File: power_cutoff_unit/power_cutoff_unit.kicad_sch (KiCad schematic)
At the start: 31 parts, among them J1 Conn_01x02, J2 Conn_01x02, J3 Conn_01x02, K1 T9GS1L14-5, U2 STM32F303K8Tx, U3 LMR50410Y5FQDBVRQ1, U4 LMR50410Y3FQDBVRQ1, U5 ADuM120N, U6 MIC4427, U7 MCP2562-E-SN

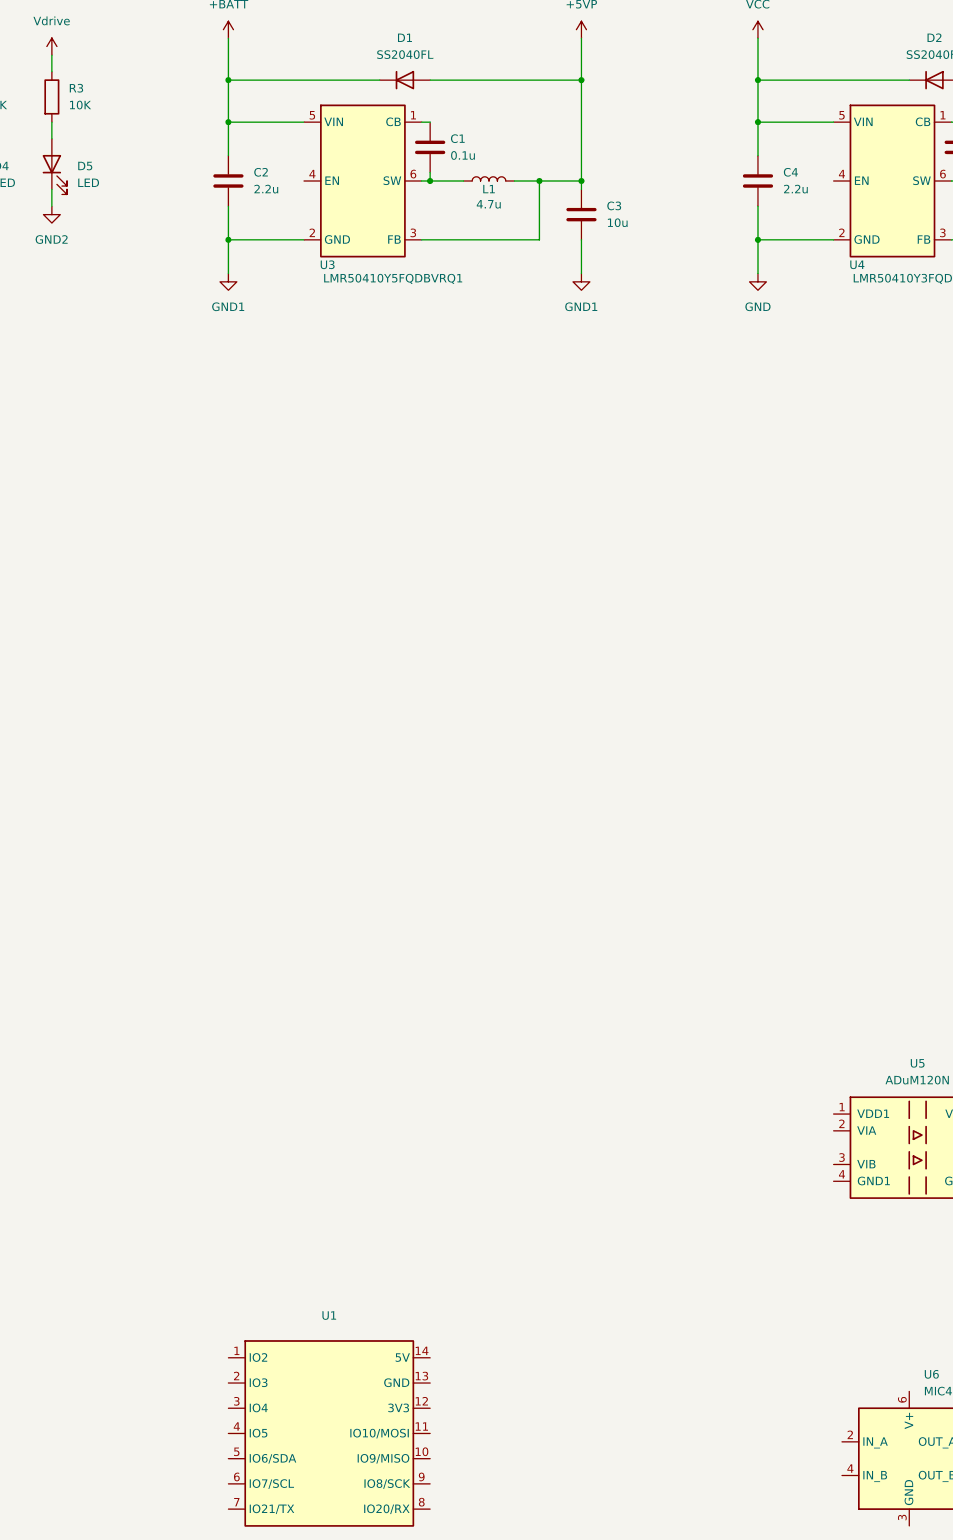
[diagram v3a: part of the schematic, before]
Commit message: 仕様書追記。リレーの追加。
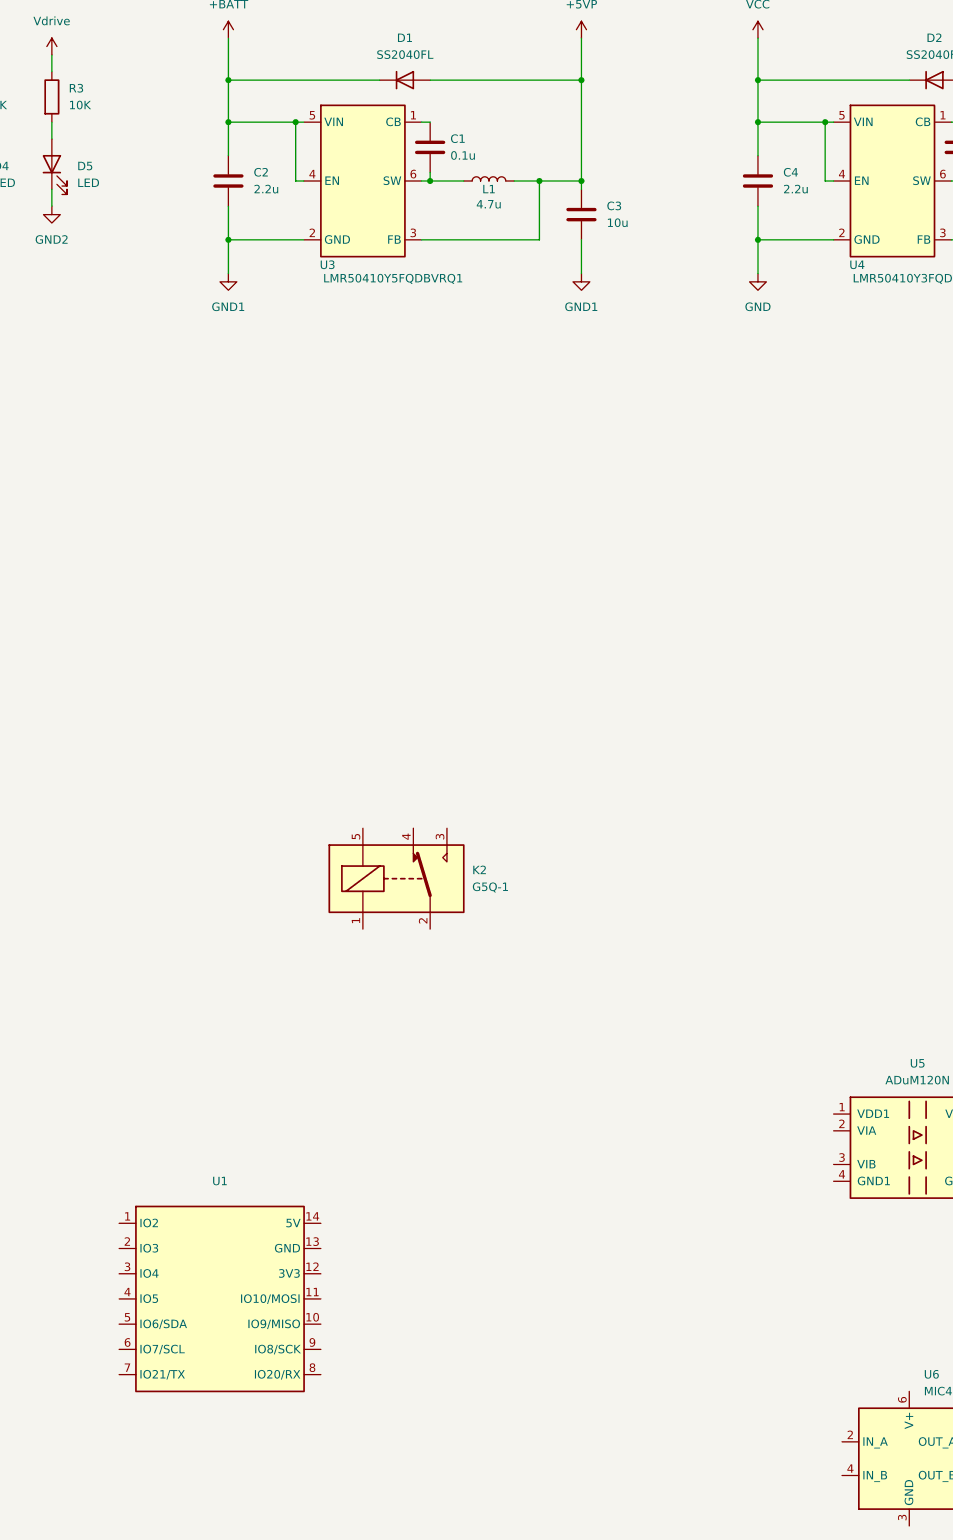
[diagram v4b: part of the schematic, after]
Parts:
- added K2: G5Q-1, Relay_THT:Relay_SPDT_Omron-G5Q-1, symbol Relay:G5Q-1
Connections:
- net +BATT: now also U3.4 (EN)
- net VCC: now also U4.4 (EN)
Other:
- moved on the sheet: U1
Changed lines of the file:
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@@
+	)
+	(junction
+		(at 243.84 38.1)
+		(diameter 0)
+		(color 0 0 0 0)
 	)
 	(junction
@@
 	)
 	(junction
+		(at 163.83 38.1)
+		(diameter 0)
+		(color 0 0 0 0)
+	)
+	(junction
 		(at 287.02 31.75)
 		(diameter 0)
@@
 	(wire
 		(pts
-			(xy 153.67 38.1) (xy 165.1 38.1)
+			(xy 153.67 38.1) (xy 163.83 38.1)
 		)
 		(stroke
@@
 	(wire
 		(pts
+			(xy 163.83 46.99) (xy 163.83 38.1)
+		)
+		(stroke
+			(width 0)
+			(type default)
+		)
+	)
+	(wire
+		(pts
 			(xy 262.89 55.88) (xy 280.67 55.88)
 		)
@@
 	(wire
 		(pts
+			(xy 243.84 38.1) (xy 245.11 38.1)
+		)
+		(stroke
+			(width 0)
+			(type default)
+		)
+	)
+	(wire
+		(pts
 			(xy 184.15 45.72) (xy 184.15 46.99)
 		)
@@
 	(wire
 		(pts
+			(xy 163.83 38.1) (xy 165.1 38.1)
+		)
+		(stroke
+			(width 0)
+			(type default)
+		)
+	)
+	(wire
+		(pts
 			(xy 102.87 27.94) (xy 102.87 30.48)
 		)
@@
 	(wire
 		(pts
+			(xy 243.84 46.99) (xy 243.84 38.1)
+		)
+		(stroke
+			(width 0)
+			(type default)
+		)
+	)
+	(wire
+		(pts
+			(xy 245.11 46.99) (xy 243.84 46.99)
+		)
+		(stroke
+			(width 0)
+			(type default)
+		)
+	)
+	(wire
+		(pts
+			(xy 165.1 46.99) (xy 163.83 46.99)
+		)
+		(stroke
+			(width 0)
+			(type default)
+		)
+	)
+	(wire
+		(pts
 			(xy 64.77 43.18) (xy 64.77 48.26)
 		)
@@
 	(wire
 		(pts
-			(xy 233.68 38.1) (xy 245.11 38.1)
+			(xy 233.68 38.1) (xy 243.84 38.1)
 		)
 		(stroke
@@
 	)
 	(symbol
+		(lib_id "Relay:G5Q-1")
+		(at 179.07 152.4 0)
+		(unit 1)
+		(exclude_from_sim no)
+		(in_bom yes)
+		(on_board yes)
+		(dnp no)
+		(fields_autoplaced yes)
+		(property "Reference" "K2"
+			(at 190.5 151.1299 0)
+			(effects
+				(font
+					(size 1.27 1.27)
+				)
+				(justify left)
+			)
+		)
+		(property "Value" "G5Q-1"
+			(at 190.5 153.6699 0)
+			(effects
+				(font
+					(size 1.27 1.27)
+				)
+				(justify left)
+			)
+		)
+		(property "Footprint" "Relay_THT:Relay_SPDT_Omron-G5Q-1"
+			(at 190.5 153.67 0)
+			(effects
+				(font
+					(size 1.27 1.27)
+				)
+				(justify left)
+				(hide yes)
+			)
+		)
+		(property "Datasheet" "https://www.omron.com/ecb/products/pdf/en-g5q.pdf"
+			(at 179.07 152.4 0)
+			(effects
+				(font
+					(size 1.27 1.27)
+				)
+				(justify left)
+				(hide yes)
+			)
+		)
+		(property "Description" "Omron G5G relay, Miniature Single Pole, SPDT, 10A"
+			(at 179.07 152.4 0)
+			(effects
+				(font
+					(size 1.27 1.27)
+				)
+				(hide yes)
+			)
+		)
+		(pin "4"
+		)
+		(pin "2"
+		)
+		(pin "1"
+		)
+		(pin "5"
+		)
+		(pin "3"
+		)
+		(instances
+			(project ""
+				(path "/24fe50da-72e0-4baa-9f8a-567f58795612"
+					(reference "K2")
+					(unit 1)
+				)
+			)
+		)
+	)
+	(symbol
 		(lib_id "Seed_XIAO:XIAO_ESP32C3")
-		(at 168.91 236.22 0)
+		(at 152.4 215.9 0)
 		(unit 1)
 		(exclude_from_sim no)
@@
 		(fields_autoplaced yes)
 		(property "Reference" "U1"
-			(at 168.91 218.44 0)
+			(at 152.4 198.12 0)
 			(effects
 				(font
@@
 		)
 		(property "Value" "~"
-			(at 168.91 220.98 0)
+			(at 152.4 200.66 0)
 			(effects
 				(font
@@
 		)
 		(property "Footprint" "RF_Module:MCU_Seeed_ESP32C3"
-			(at 162.56 231.14 0)
+			(at 146.05 210.82 0)
 			(effects
 				(font
@@
 		)
 		(property "Datasheet" ""
-			(at 162.56 231.14 0)
+			(at 146.05 210.82 0)
 			(effects
 				(font
@@
 		)
 		(property "Description" ""
-			(at 162.56 231.14 0)
-			(effects
-				(font
+			(at 146.05 210.82 0)
+			(effects
+				(font

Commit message: リレーの回路を組み立てた。
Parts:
- added C10, C8: C_Polarized, symbol Device:C_Polarized
- added C11, C12, C7, C9: C, symbol Device:C
- added D10, D12, D13, D9: LED, symbol Device:LED
- added D11, D8: D, symbol Device:D
- added J4, J5: Conn_01x02, symbol Connector_Generic:Conn_01x02
- added J6: Conn_01x02_Pin, symbol Connector:Conn_01x02_Pin
- added Q1, Q2, Q3: NMOS, symbol Simulation_SPICE:NMOS
- added R10, R11, R12, R13, R14, R15, R16, R17, R18, R6, R7, R8, R9: R, symbol Device:R
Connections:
- net +3.3V: now also U7.5 (Vio), C11.1
- net +5VP: now also K1.1, D8.1 (K)
- net +BATT: now also K1.3
- net GND: now also U7.2 (VSS), U7.8 (STBY), C11.2, C12.2
- net GND1: now also C7.2, C8.2, D9.1 (K), J4.1 (Pin_1), Q1.3 (S), Q2.3 (S), R10.1, R6.2
- net GND2: now also C10.2, C9.2, D12.1 (K), D13.1 (K), J5.1 (Pin_1), Q3.3 (S), R14.2, R15.2
- net Vdrive: now also K2.3, K2.5, D11.1 (K)
- net +5V: now reaches U7.3 (VDD)
- net +5V: now also C12.1
- net at U7.6 (CANL): now also R18.2
- net at U7.7 (CANH): now also J6.2 (Pin_2)
- net at K1.2: now also C7.1, C8.1, J4.2 (Pin_2), R11.2, R12.2, R8.1
- net at K1.5: now also D8.2 (A), Q1.1 (D)
- net at K2.1: now also D11.2 (A), Q3.1 (D)
- net at K2.2: now also C10.1, C9.1, J5.2 (Pin_2), R17.1
- net at K2.4: now also R15.1, R16.1
- new net: Q2.2 (G), R10.2, R9.2
- new net: Q1.2 (G), R6.1, R7.2
- new net: D12.2 (A), R16.2
- new net: Q3.2 (G), R13.2, R14.1
- new net: D10.2 (A), R12.1
- new net: J6.1 (Pin_1), R18.1
- new net: D10.1 (K), Q2.1 (D), R11.1
- new net: D13.2 (A), R17.2
- new net: D9.2 (A), R8.2
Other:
- moved on the sheet: K1, K2, U7

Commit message: Good bye ESP32 !!!!!!!
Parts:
- removed U1: ~, RF_Module:MCU_Seeed_ESP32C3, symbol Seed_XIAO:XIAO_ESP32C3
- added C13, C14, C15, C16, C17: C, symbol Device:C
- added JP1, JP2, JP3: SolderJumper_2_Open, symbol Jumper:SolderJumper_2_Open
- added R19: R, symbol Device:R
- added SW1: SW_Push, symbol Switch:SW_Push
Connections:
- net +3.3V: now also U2.1 (VDD), U2.17 (VDD), C13.1, C14.1, C15.1, JP1.2 (B), JP2.2 (B)
- net GND: now also C13.2, C14.2, C15.2, C16.2, C17.2, JP3.1 (A), R19.2, SW1.1
- net PB0: now reaches U2.14 (PB0)
- net PB0: now also JP3.2 (B)
- net PB1: now reaches U2.15 (PB1)
- net PB1: now also C17.1, JP2.1 (A)
- net at U2.31 (BOOT0): now also R19.1
- net NRST: now reaches U2.4 (NRST)
- net NRST: now also C16.1, SW1.2
- net at U2.5 (VDDA): now also JP1.1 (A)
- no-connect marks 0 -> 2

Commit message: add: RNBD451
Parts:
- added C18, C21: 4.7u, symbol Device:C
- added C19, C20: 0.1u, symbol Device:C
- added C22, C23: 18p, symbol Device:C
- added U1: RNBD451, symbol GN10_Parts:RNBD451
- added Y1: 32.768K, symbol Device:Crystal
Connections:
- net +3.3V: now also C18.1, C19.1, C20.1, C21.1, U1.27 (VDD), U1.28 (VDD), U1.7 (VDD_A)
- net GND: now also C18.2, C19.2, C20.2, C21.2, C22.1, C23.2, U1.1 (GND), U1.11 (GND), U1.19 (GND), U1.2 (GND), U1.26 (GND), U1.40 (TPAD_GND), U1.8 (GND)
- new net: C23.1, U1.10 (PA12), Y1.2
- new net: C22.2, U1.9 (PA11), Y1.1
- new net BLE_DEBUG_RX: U1.29 (PA8)
- new net BLE_DEBUG_TX: U1.31 (PA7)
- new net BLE_RESET: U1.3 (NMCLR)
- new net BLE_RSSI_LED: U1.36 (PA3)
- new net BLE_STATUS_1: U1.5 (PB3)
- new net BLE_STATUS_2: U1.13 (PB7)
- new net BLE_STATUS_LED: U1.6 (PB5)
- new net BLE_STATUS_UART_RX: U1.15 (PB9)
- new net BLE_STATUS_UART_TX: U1.35 (PA2)
- new net BLE_UART_CTS: U1.25 (PA6)
- new net BLE_UART_MODE_SW: U1.37 (PB2)
- new net BLE_UART_RX: U1.12 (PB6)
- new net BLE_UART_RX_LED: U1.39 (PB4)
- new net BLE_UART_TX: U1.24 (PA5)
- new net WRAN_ACTIVE: U1.4 (PB0)
- no-connect marks 2 -> 15
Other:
- moved on the sheet: C11, C12, J6, R18, U5, U6, U7

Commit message: RNBD451のFPを作ってる。
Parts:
- U1: footprint (none) -> GN10_Parts:ZSX
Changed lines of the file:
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@@
 			)
 		)
-		(property "Footprint" ""
+		(property "Footprint" "GN10_Parts:ZSX"
 			(at 151.13 321.31 0)
 			(effects
